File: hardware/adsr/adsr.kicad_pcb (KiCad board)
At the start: 4 copper layers, 29 x 100 mm, 87 parts, among them J1 MonoJack, J2 MonoJack, J3 MonoJack, J4 Conn_02x05_Odd_Even, Q1 BC847, Q2 BC847, Q3 BC847, Q4 BC847, Q5 BC847, Q6 BC847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

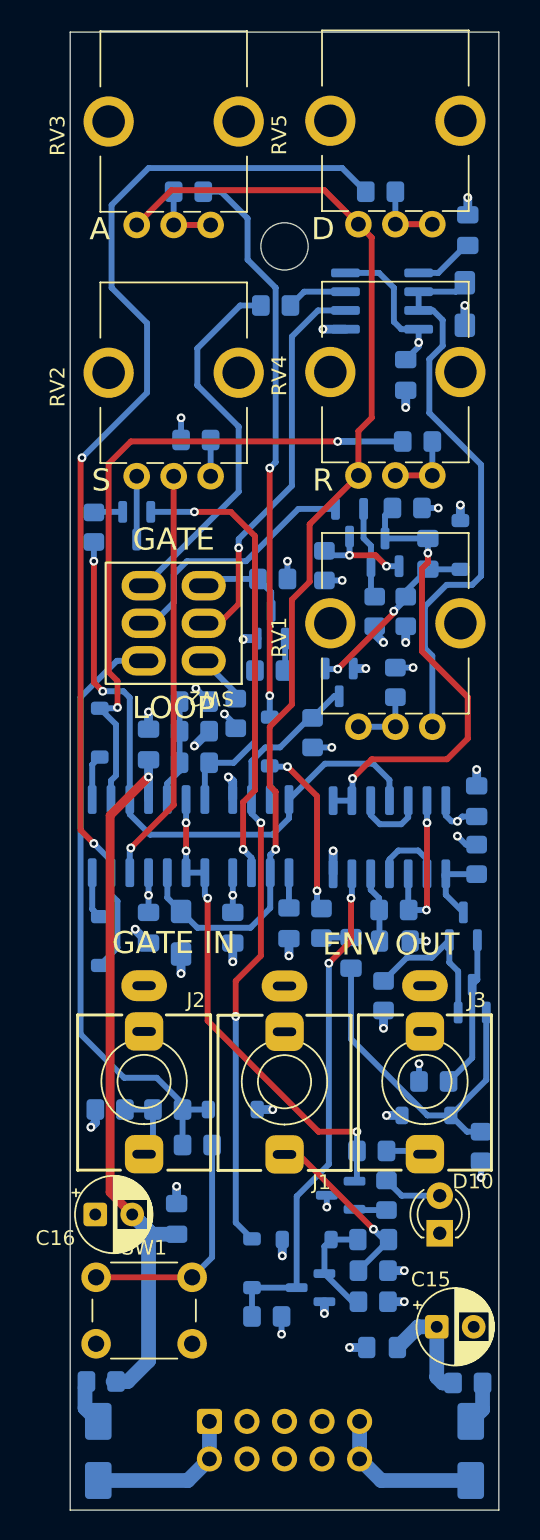
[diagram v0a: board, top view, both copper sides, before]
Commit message: clean up silk, check board, generate gerbers for v2
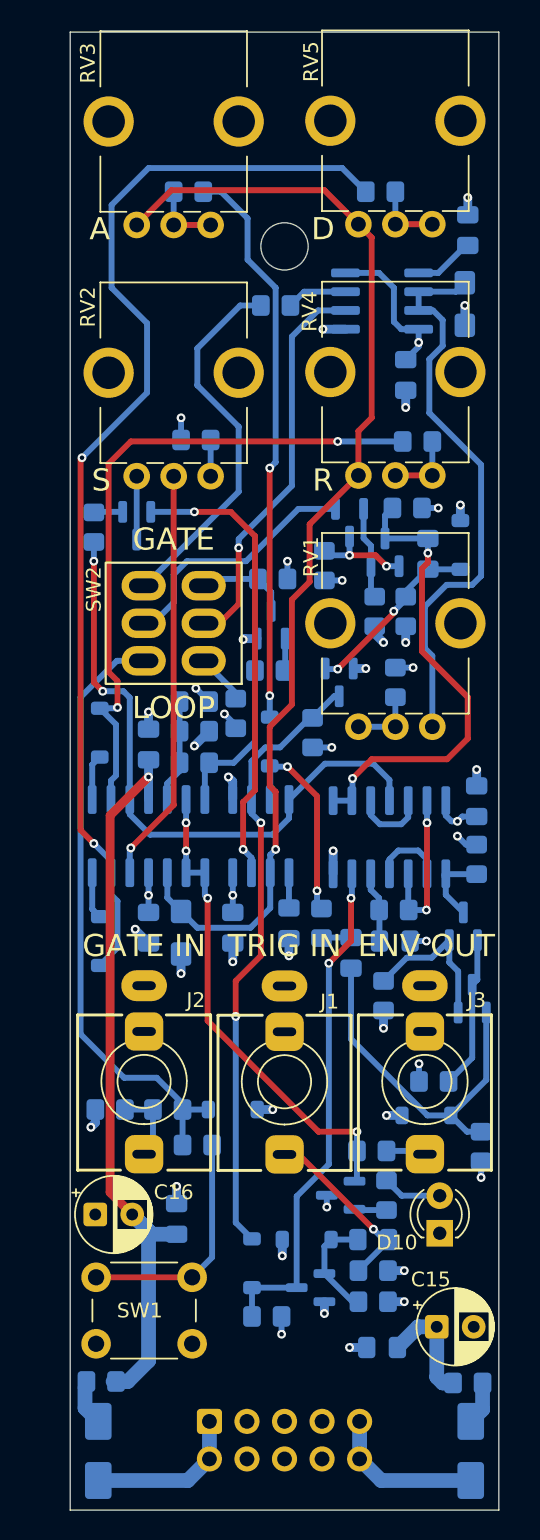
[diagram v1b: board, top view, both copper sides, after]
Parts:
- C2, C8: value 4U7 -> 4u7
- R14: value 10 -> 10R
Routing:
- net Net-(D7-A): track 46.5 -> 45.3 mm
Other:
- board text added: "TRIG IN"
- board text added: "v2.0.20251123 idyllm CC BY-SA 4.0"
- board text removed: "v1.0.20250922 idyllm CC BY-SA 4.0"
